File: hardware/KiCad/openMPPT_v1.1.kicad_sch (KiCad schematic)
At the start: 0 parts

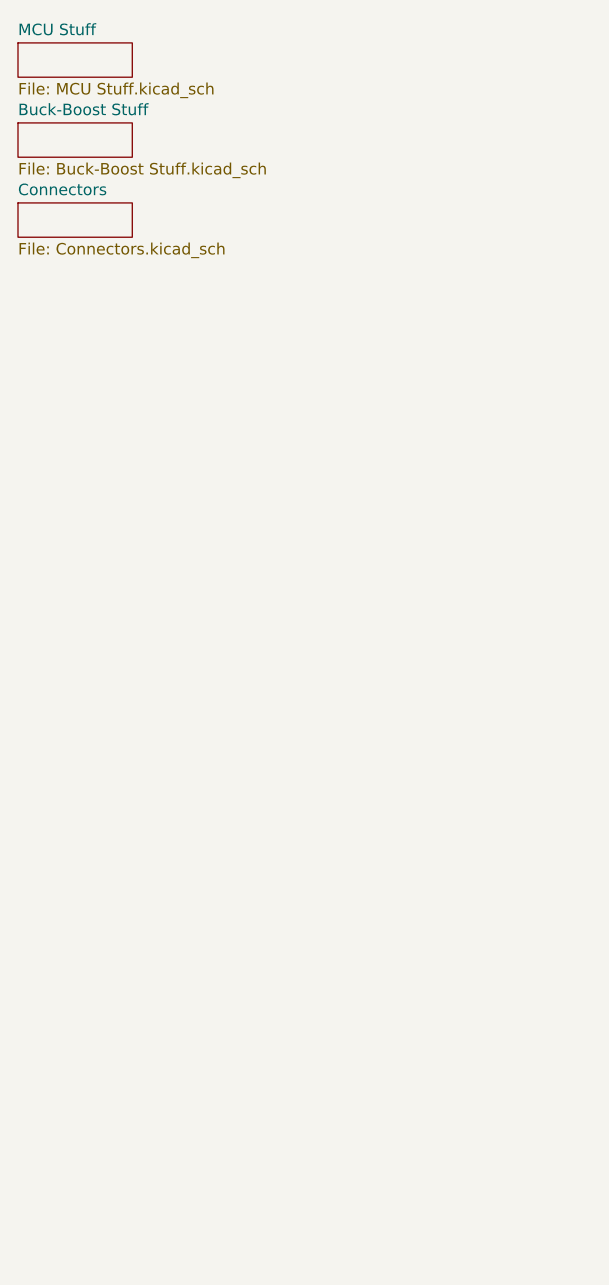
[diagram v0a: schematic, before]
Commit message: added the new 10v regulator
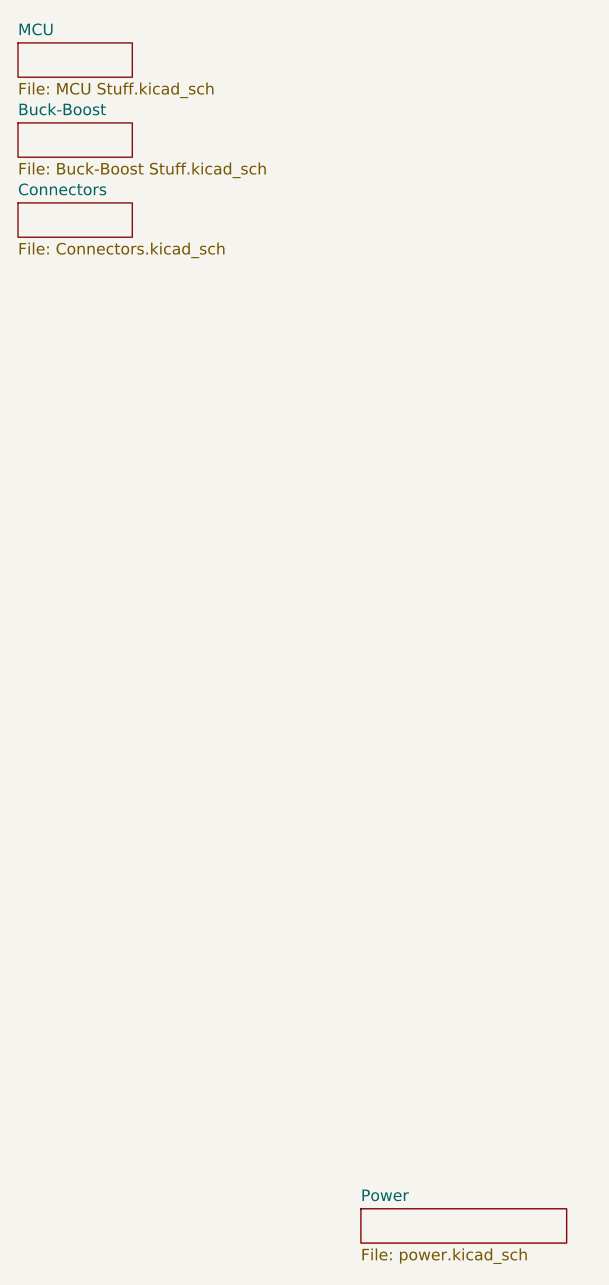
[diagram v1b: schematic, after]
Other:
- sheet Buck-Boost Stuff renamed Buck-Boost
- sheet MCU Stuff renamed MCU
- added sheet Power (power.kicad_sch)
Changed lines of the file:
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@@
 			(color 0 0 0 0)
 		)
-		(property "Sheetname" "Buck-Boost Stuff"
+		(property "Sheetname" "Buck-Boost"
 			(at 27.94 33.5784 0)
 			(show_name no)
@@
 			(color 0 0 0 0)
 		)
-		(property "Sheetname" "MCU Stuff"
+		(property "Sheetname" "MCU"
 			(at 27.94 24.6884 0)
 			(show_name no)
@@
 				)
 			)
+		)
+	)
+	(sheet
+		(at 66.04 154.94)
+		(size 22.86 3.81)
+		(exclude_from_sim no)
+		(in_bom yes)
+		(on_board yes)
+		(dnp no)
+		(fields_autoplaced yes)
+		(stroke
+			(width 0.1524)
+			(type solid)
+		)
+		(fill
+			(color 0 0 0 0)
+		)
+		(property "Sheetname" "Power"
+			(at 66.04 154.2284 0)
+			(show_name no)
+			(do_not_autoplace no)
+			(effects
+				(font
+					(size 1.27 1.27)
+				)
+				(justify left bottom)
+			)
+		)
+		(property "Sheetfile" "power.kicad_sch"
+			(at 66.04 159.3346 0)
+			(show_name no)
+			(do_not_autoplace no)
+			(effects
+				(font
+					(size 1.27 1.27)
+				)
+				(justify left top)
+			)
+		)
+		(instances
+			(project "openMPPT_v1.1"
+				(path "/f6f5d1da-a682-42b4-8a9f-7d9a10833a0c"
+					(page "4")
+				)
+			)
